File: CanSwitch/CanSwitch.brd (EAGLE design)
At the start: 64.8 x 80 mm, 17 parts

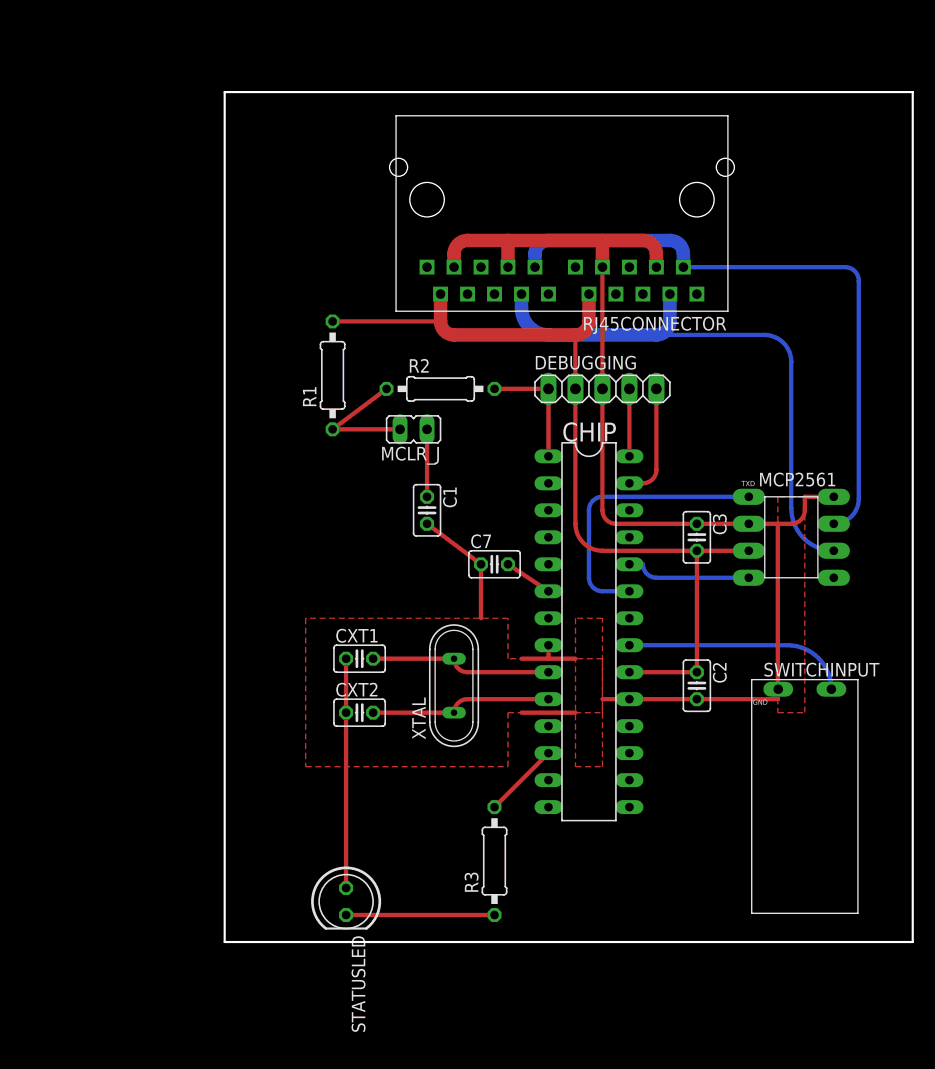
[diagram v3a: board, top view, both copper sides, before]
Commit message: #2 renamed few components, moved all to new origin, added holes for final drilling, added silkcreen to desc all, including signature. Not to print out names layers, only place and values layers in the final silkscreen
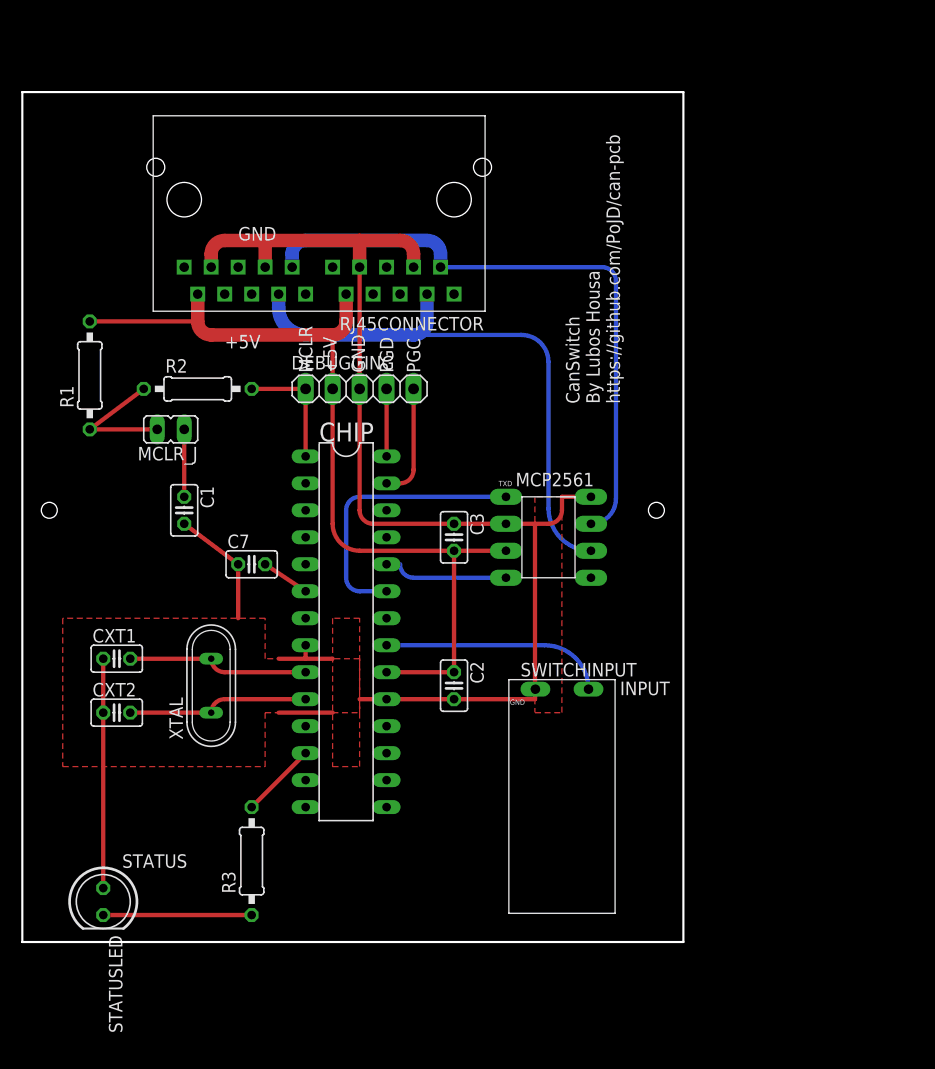
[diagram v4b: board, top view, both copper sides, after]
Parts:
- R1: value 10kOhm -> 10000
- R2: value 470Ohm -> 470
- R3: value 1kOhm -> 1000
- moved C7 22.9 mm to (21.6, 35.6)
- moved CHIP 22.9 mm to (30.5, 29.2)
- moved R3 22.9 mm to (21.6, 7.62)
- moved C1 22.9 mm to (15.2, 40.6)
- moved C2 22.9 mm to (40.6, 24.1)
- moved C3 22.9 mm to (40.6, 38.1)
- moved CXT1 22.9 mm to (8.89, 26.7)
- moved CXT2 22.9 mm to (8.89, 21.6)
- moved DEBUGGING 22.9 mm to (31.8, 52.1)
- moved MCLR_J 22.9 mm to (14.0, 48.3)
- moved MCP2561 22.9 mm to (49.5, 38.1)
- moved R1 22.9 mm to (6.35, 53.3)
- moved STATUSLED 22.9 mm to (7.62, 3.81)
- moved SWITCHINPUT 22.9 mm to (50.8, 12.7)
- moved XTAL 22.9 mm to (17.8, 24.1)
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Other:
- board size 64.8 x 80 mm -> 62.2 x 80 mm
- board text added: "+5V"
- board text added: "CANH"
- board text added: "CANL"
- board text added: "CanSwitch By Lubos Housa https://github.com/PoJD/can-pcb"
- board text added: "GND"
- board text added: "INPUT"
- board text added: "MCLR"
- board text added: "PGC"
- board text added: "PGD"
- board text added: "STATUS"

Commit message: moving capacitor a bit further from the chip
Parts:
- moved C7 2.54 mm to (19.1, 35.6)
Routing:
- net N$4: track 4.58 -> 6.84 mm
- net GND: track 152.1 -> 150.3 mm
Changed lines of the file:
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@@
 <layer number="43" name="vRestrict" color="2" fill="10" visible="yes" active="yes"/>
 <layer number="44" name="Drills" color="7" fill="1" visible="yes" active="yes"/>
-<layer number="45" name="Holes" color="7" fill="1" visible="no" active="yes"/>
+<layer number="45" name="Holes" color="7" fill="1" visible="yes" active="yes"/>
 <layer number="46" name="Milling" color="3" fill="1" visible="yes" active="yes"/>
 <layer number="47" name="Measures" color="7" fill="1" visible="yes" active="yes"/>
@@
 <element name="C1" library="rcl" package="C025-025X050" value="0.1uF" x="15.24" y="40.64" rot="R270"/>
 <element name="C2" library="rcl" package="C025-025X050" value="0.1uF" x="40.64" y="24.13" rot="R270"/>
-<element name="C7" library="rcl" package="C025-025X050" value="10 uF" x="21.59" y="35.56"/>
+<element name="C7" library="rcl" package="C025-025X050" value="10 uF" x="19.05" y="35.56"/>
 <element name="CHIP" library="microchip" package="DIL28-3" value="PIC18F2480-I/SP" x="30.48" y="29.21" rot="R270">
 <attribute name="MPN" value="PIC18F2480-I/SP" x="30.48" y="29.21" size="1.778" layer="27" rot="R270" display="off"/>
@@
 <wire x1="31.75" y1="63.53" x2="31.75" y2="66.04" width="1.27" layer="1"/>
 <wire x1="7.62" y1="26.67" x2="7.62" y2="21.59" width="0.4064" layer="1"/>
-<wire x1="20.32" y1="35.56" x2="20.32" y2="30.48" width="0.4064" layer="1"/>
-<wire x1="15.24" y1="39.37" x2="20.32" y2="35.56" width="0.4064" layer="1"/>
+<wire x1="17.78" y1="35.56" x2="17.78" y2="30.48" width="0.4064" layer="1"/>
+<wire x1="15.24" y1="39.37" x2="17.78" y2="35.56" width="0.4064" layer="1"/>
 <polygon width="0.4064" layer="1" isolate="0.6096">
 <vertex x="3.81" y="30.48"/>
@@
 <contactref element="CHIP" pad="6"/>
 <contactref element="C7" pad="2"/>
-<wire x1="26.67" y1="33.02" x2="22.86" y2="35.56" width="0.4064" layer="1"/>
+<wire x1="26.67" y1="33.02" x2="20.32" y2="35.56" width="0.4064" layer="1"/>
 </signal>
 <signal name="N$6">

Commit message: #1 dropping old polygons and replacing with full board ground polygons on both sides with isolation spacing 0.4
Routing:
- net GND: track 150.3 -> 131.8 mm
- net CANH: track 58.4 -> 60.4 mm
- added copper zone on layer 16, net GND
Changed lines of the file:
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@@
 <setting verticaltext="up"/>
 </settings>
-<grid distance="1.27" unitdist="mm" unit="mm" style="lines" multiple="1" display="yes" altdistance="0.3175" altunitdist="mm" altunit="mm"/>
+<grid distance="1.27" unitdist="mm" unit="mm" style="lines" multiple="1" display="yes" altdistance="0.01" altunitdist="mm" altunit="mm"/>
 <layers>
 <layer number="1" name="Top" color="4" fill="1" visible="yes" active="yes"/>
@@
 <wire x1="7.62" y1="26.67" x2="7.62" y2="21.59" width="0.4064" layer="1"/>
 <wire x1="17.78" y1="35.56" x2="17.78" y2="30.48" width="0.4064" layer="1"/>
-<wire x1="15.24" y1="39.37" x2="17.78" y2="35.56" width="0.4064" layer="1"/>
-<polygon width="0.4064" layer="1" isolate="0.6096">
-<vertex x="3.81" y="30.48"/>
-<vertex x="3.81" y="16.51"/>
-<vertex x="22.86" y="16.51"/>
-<vertex x="22.86" y="21.59"/>
-<vertex x="31.75" y="21.59"/>
-<vertex x="31.75" y="26.67"/>
-<vertex x="22.86" y="26.67"/>
-<vertex x="22.86" y="30.48"/>
-</polygon>
-<polygon width="0.4064" layer="1" isolate="0.6096">
-<vertex x="29.21" y="30.48"/>
-<vertex x="29.21" y="16.51"/>
-<vertex x="31.75" y="16.51"/>
-<vertex x="31.75" y="30.48"/>
-</polygon>
-<wire x1="34.29" y1="22.86" x2="31.75" y2="22.86" width="0.4064" layer="1"/>
-<wire x1="24.13" y1="26.67" x2="26.67" y2="26.67" width="0.4064" layer="1"/>
-<wire x1="26.67" y1="26.67" x2="29.21" y2="26.67" width="0.4064" layer="1"/>
-<wire x1="24.13" y1="21.59" x2="29.21" y2="21.59" width="0.4064" layer="1"/>
-<wire x1="26.67" y1="27.94" x2="26.67" y2="26.67" width="0.4064" layer="1"/>
-<polygon width="0.4064" layer="1" isolate="0.6096">
-<vertex x="48.26" y="41.91"/>
-<vertex x="48.26" y="21.59"/>
-<vertex x="50.8" y="21.59"/>
-<vertex x="50.8" y="41.91"/>
-</polygon>
 <wire x1="40.64" y1="22.86" x2="48.26" y2="22.86" width="0.4064" layer="1"/>
 <wire x1="48.26" y1="22.86" x2="48.3" y2="23.8" width="0.4064" layer="1"/>
 <wire x1="50.8" y1="41.91" x2="50.8" y2="40.64" width="0.4064" layer="1"/>
+<polygon width="0.4064" layer="1" spacing="0.254" isolate="0.4064">
+<vertex x="1.27" y="78.74"/>
+<vertex x="60.96" y="78.74"/>
+<vertex x="60.96" y="1.27"/>
+<vertex x="1.27" y="1.27"/>
+</polygon>
+<polygon width="0.4064" layer="16" spacing="0.254" isolate="0.4064">
+<vertex x="1.27" y="78.74"/>
+<vertex x="60.96" y="78.74"/>
+<vertex x="60.96" y="1.27"/>
+<vertex x="1.27" y="1.27"/>
+</polygon>
 </signal>
 <signal name="N$2">
@@
 <wire x1="39.37" y1="64.77" x2="38.1" y2="66.04" width="1.27" layer="16" curve="90"/>
 <wire x1="39.37" y1="63.53" x2="54.58" y2="63.53" width="0.4064" layer="16"/>
-<wire x1="54.58" y1="63.53" x2="55.88" y2="62.23" width="0.4064" layer="16" curve="-90"/>
-<wire x1="55.88" y1="62.23" x2="55.88" y2="41.72" width="0.4064" layer="16"/>
-<wire x1="55.88" y1="41.72" x2="53.53" y2="39.37" width="0.4064" layer="16" curve="-90"/>
+<wire x1="54.58" y1="63.53" x2="57.15" y2="62.23" width="0.4064" layer="16" curve="-90"/>
+<wire x1="57.15" y1="62.23" x2="57.15" y2="41.72" width="0.4064" layer="16"/>
+<wire x1="57.15" y1="41.72" x2="53.53" y2="39.37" width="0.4064" layer="16" curve="-90"/>
 </signal>
 <signal name="CANL">

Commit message: #5 new component for RJ45 WEBPP single, also renamed old one to DOUBLE and updated CanSwitch project references, used in CanRelay now and added all the wiring to it too
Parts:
- RJ45CONNECTOR: value WEBP88GME -> WEBP88_DDOUBLE; device PoJD:WEBP88_RJ45 -> PoJD:WEBP88_RJ45_DOUBLE
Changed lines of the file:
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@@
 <element name="R2" library="rcl" package="0207/10" value="470" x="16.51" y="52.07"/>
 <element name="R3" library="rcl" package="0207/10" value="1000" x="21.59" y="7.62" rot="R90"/>
-<element name="RJ45CONNECTOR" library="PoJD" package="WEBP88_RJ45" value="WEBP88GME" x="27.94" y="68.58" rot="R180"/>
+<element name="RJ45CONNECTOR" library="PoJD" package="WEBP88_RJ45_DOUBLE" value="WEBP88_DDOUBLE" x="27.94" y="68.58" rot="R180"/>
 <element name="STATUSLED" library="led" package="LED5MM" value="" x="7.62" y="3.81" rot="R270"/>
 <element name="SWITCHINPUT" library="PoJD" package="PTR_AK700_2_5.0" value="PTRAK700250GME" x="50.8" y="12.7"/>

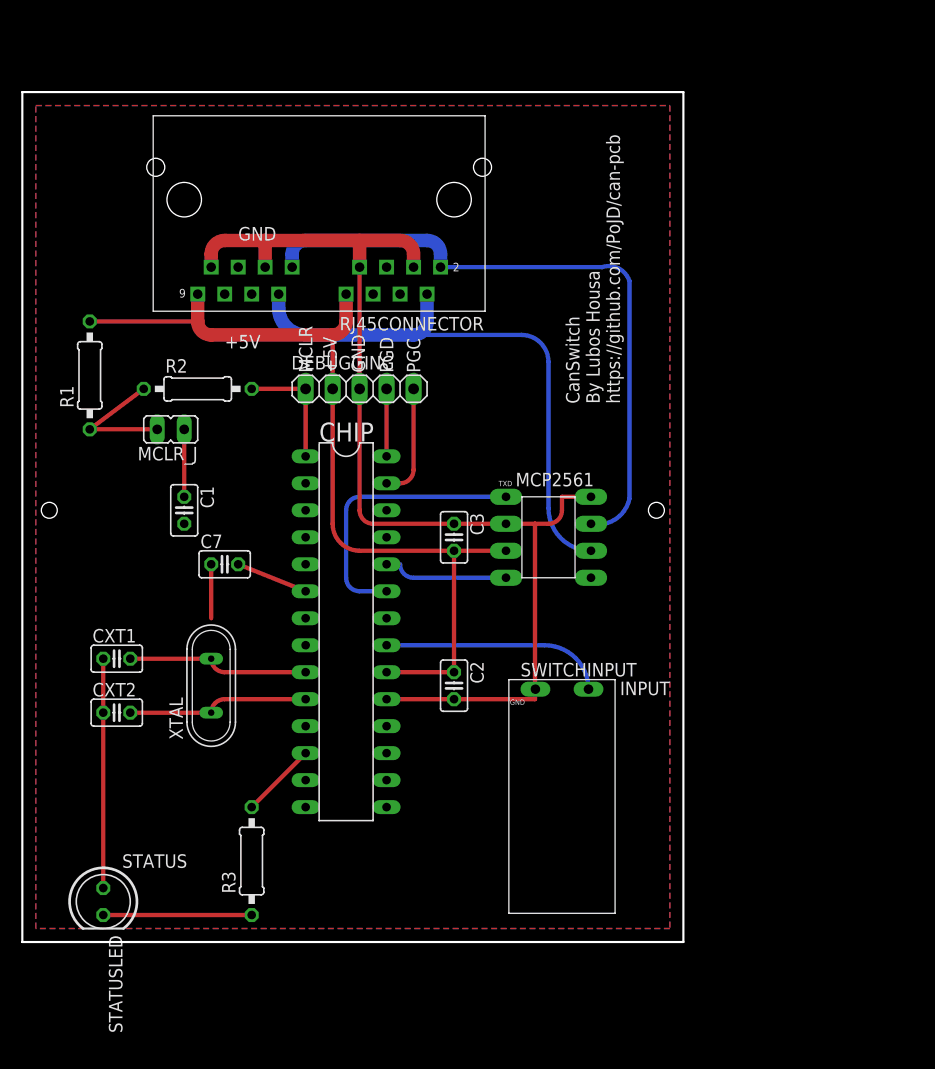
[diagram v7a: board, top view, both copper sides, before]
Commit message: first draft version of the board with routed everything and copper ground too
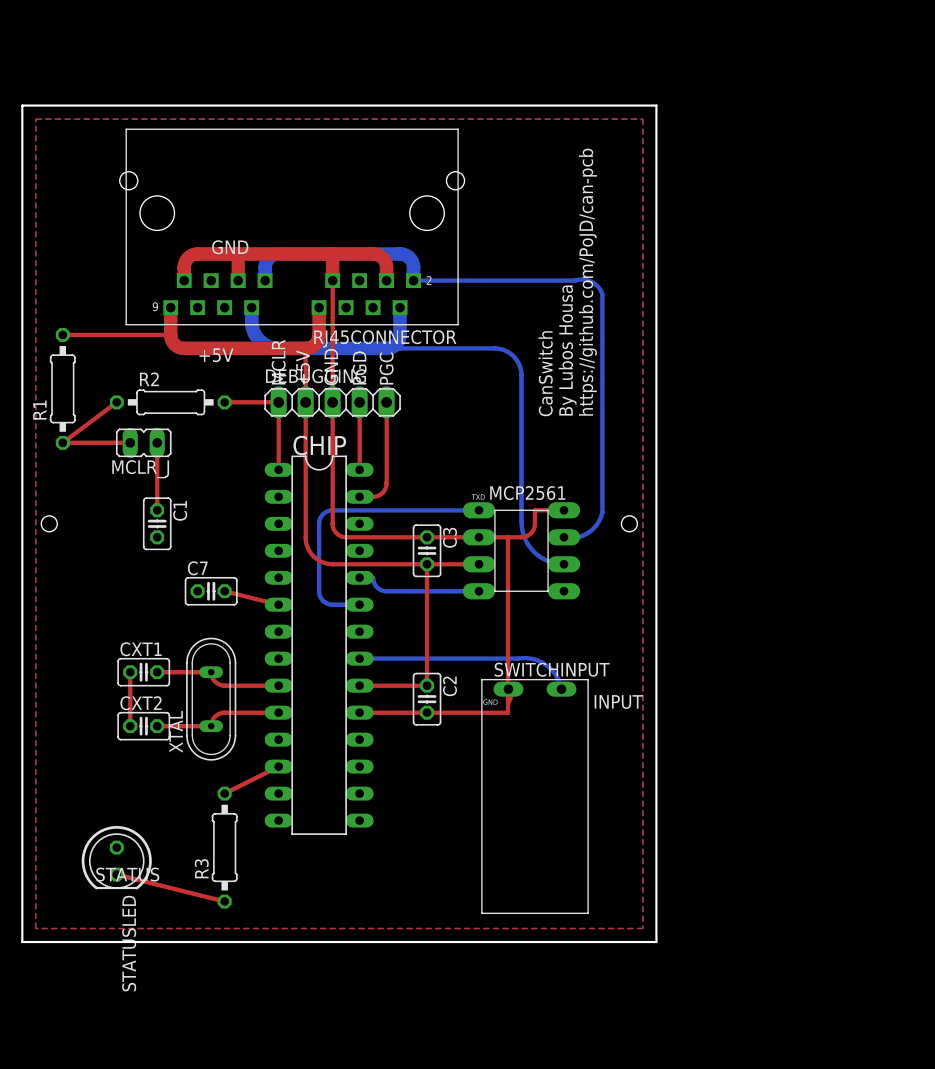
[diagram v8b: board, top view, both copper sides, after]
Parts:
- moved STATUSLED 4.02 mm to (8.89, 7.62)
- moved C1 2.84 mm to (12.7, 39.4)
- moved R2 2.84 mm to (14.0, 50.8)
- moved R1 2.84 mm to (3.81, 52.1)
- moved C3 2.84 mm to (38.1, 36.8)
- moved CXT1 2.84 mm to (11.4, 25.4)
- moved DEBUGGING 2.84 mm to (29.2, 50.8)
- moved MCP2561 2.84 mm to (47.0, 36.8)
- moved RJ45CONNECTOR 2.84 mm to (25.4, 67.3)
- moved R3 2.84 mm to (19.1, 8.89)
- moved C2 2.84 mm to (38.1, 22.9)
- moved C7 2.84 mm to (17.8, 33.0)
- moved CHIP 2.84 mm to (27.9, 27.9)
- moved CXT2 2.84 mm to (11.4, 20.3)
- moved MCLR_J 2.84 mm to (11.4, 47.0)
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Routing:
- net GND: track 131.8 -> 112.6 mm
- net N$6: track 17.0 -> 12.0 mm
- net N$3: track 17.0 -> 12.0 mm
- net N$8: track 14.0 -> 10.5 mm
- net N$4: track 6.84 -> 5.24 mm
- net N$7: track 7.18 -> 5.68 mm
- net INPUT: track 20.7 -> 19.9 mm
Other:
- board size 62.2 x 80 mm -> 59.7 x 78.7 mm
